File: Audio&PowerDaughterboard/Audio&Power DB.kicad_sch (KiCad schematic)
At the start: 7 parts, among them J1 AudioJack3, J2 AudioJack3, J3 AudioJack3, J4 USB_C_Receptacle_USB2.0, U1 SGTL5000XNLA3

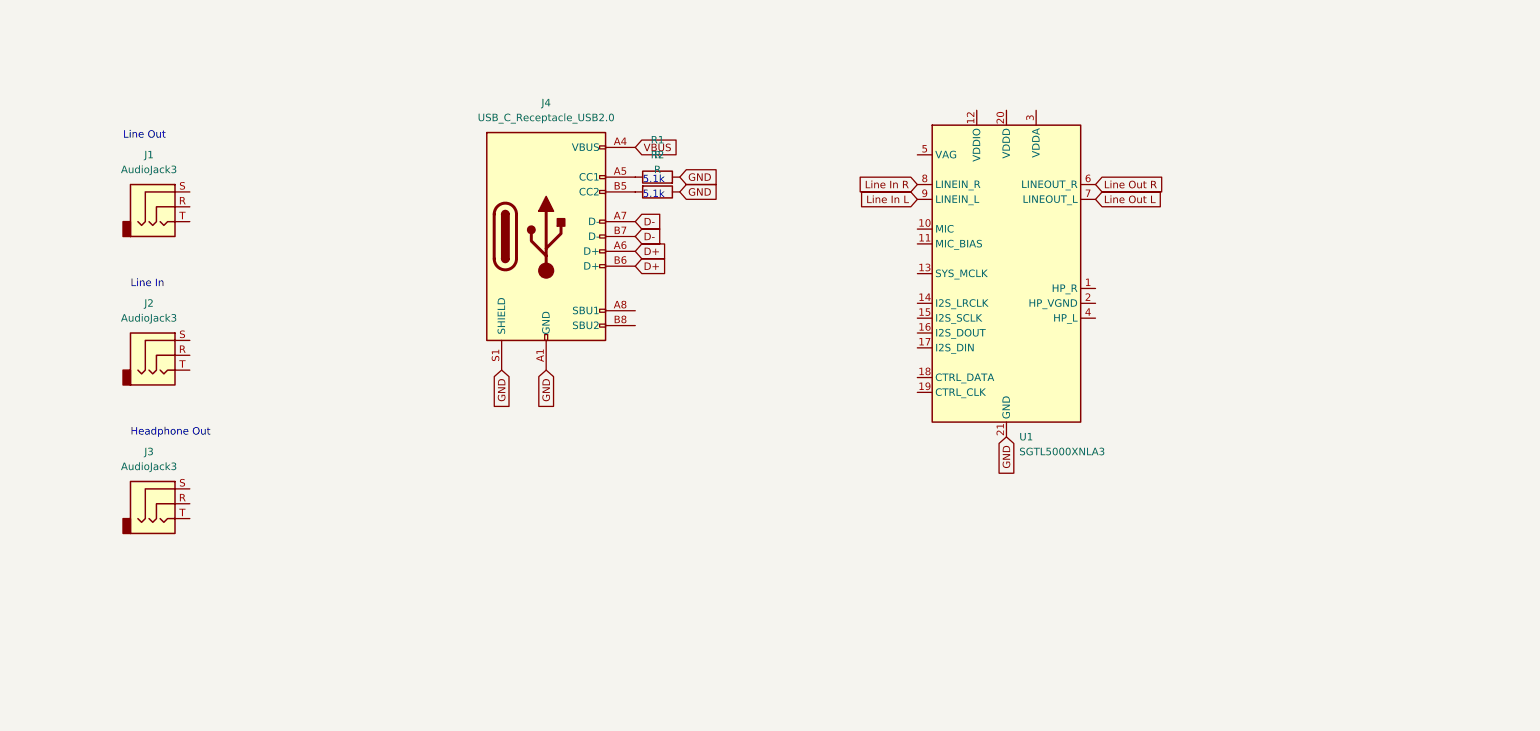
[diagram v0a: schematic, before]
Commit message: VAL FIX POWER PLS
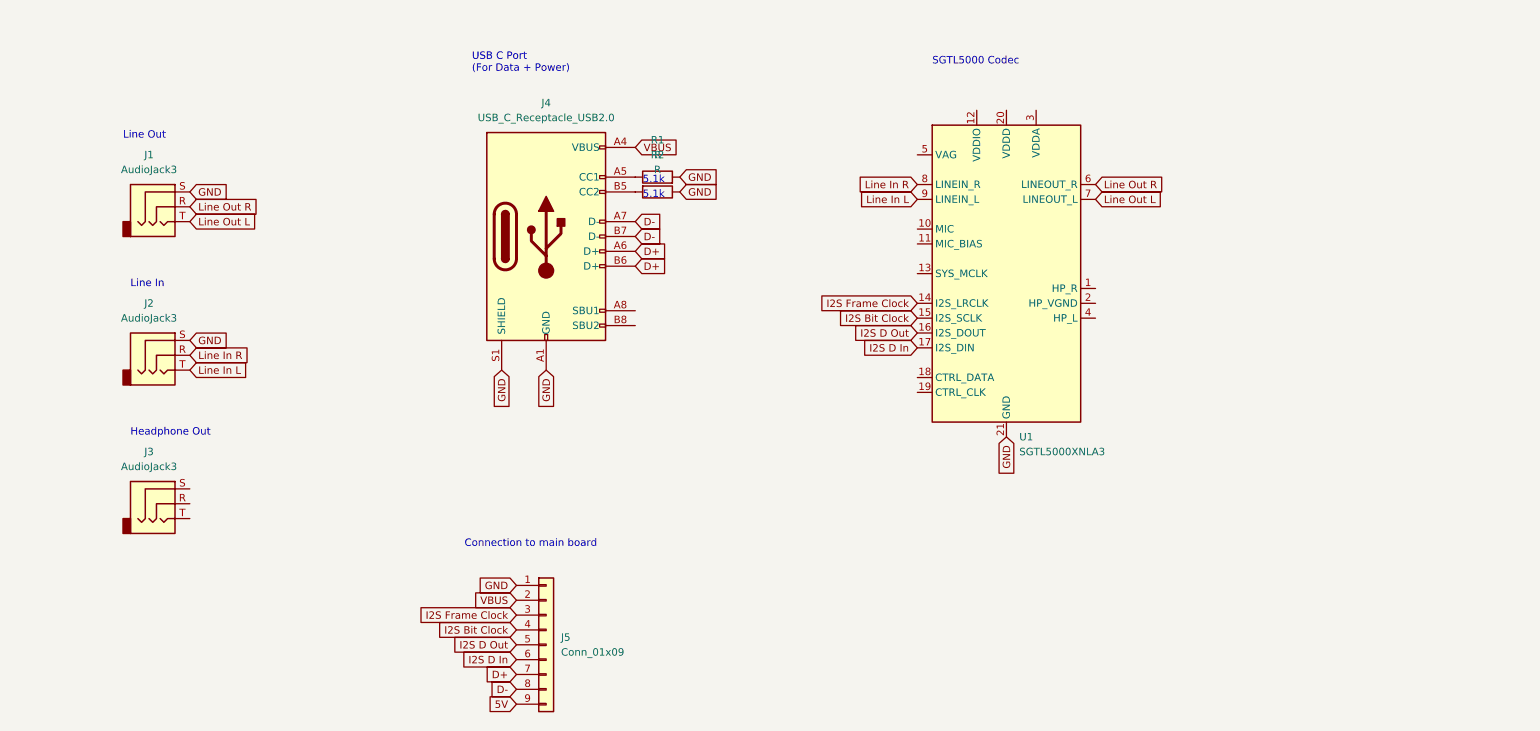
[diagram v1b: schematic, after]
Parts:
- added J5: Conn_01x09, symbol Connector_Generic:Conn_01x09
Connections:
- net D+: now also J5.7 (Pin_7)
- net D-: now also J5.8 (Pin_8)
- net GND: now also J1.S, J2.S, J5.1 (Pin_1)
- net Line In L: now also J2.T
- net Line In R: now also J2.R
- net Line Out L: now also J1.T
- net Line Out R: now also J1.R
- net VBUS: now also J5.2 (Pin_2)
- net I2S Frame Clock: now reaches U1.14 (I2S_LRCLK)
- net I2S Frame Clock: now also J5.3 (Pin_3)
- net I2S Bit Clock: now reaches U1.15 (I2S_SCLK)
- net I2S Bit Clock: now also J5.4 (Pin_4)
- net I2S D Out: now reaches U1.16 (I2S_DOUT)
- net I2S D Out: now also J5.5 (Pin_5)
- net I2S D In: now reaches U1.17 (I2S_DIN)
- net I2S D In: now also J5.6 (Pin_6)
- new net 5V: J5.9 (Pin_9)
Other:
- note added: "Connection to main board"
- note added: "SGTL5000 Codec"
- note added: "USB C Port (For Data + Power)"
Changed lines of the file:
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@@
+    (effects (font (size 1.27 1.27)) (justify left bottom))
+  )
+  (text "USB C Port\n(For Data + Power)" (at 99.06 25.4 0)
     (effects (font (size 1.27 1.27)) (justify left bottom))
   )
@@
     (effects (font (size 1.27 1.27)) (justify left bottom))
   )
+  (text "SGTL5000 Codec" (at 177.8 24.13 0)
+    (effects (font (size 1.27 1.27)) (justify left bottom))
+  )
   (text "Line Out" (at 39.37 36.83 0)
     (effects (font (size 1.27 1.27)) (justify left bottom))
   )
+  (text "Connection to main board" (at 97.79 106.68 0)
+    (effects (font (size 1.27 1.27)) (justify left bottom))
+  )
   (global_label "D-" (shape input) (at 127 53.34 0) (fields_autoplaced)
     (effects (font (size 1.27 1.27)) (justify left))
@@
     )
   )
+  (global_label "I2S D Out" (shape input) (at 175.26 69.85 180) (fields_autoplaced)
+    (effects (font (size 1.27 1.27)) (justify right))
+    (property "Intersheetrefs" "${INTERSHEET_REFS}" (at 162.8406 69.85 0)
+      (effects (font (size 1.27 1.27)) (justify right) hide)
+    )
+  )
+  (global_label "I2S Bit Clock" (shape input) (at 106.68 120.65 180) (fields_autoplaced)
+    (effects (font (size 1.27 1.27)) (justify right))
+    (property "Intersheetrefs" "${INTERSHEET_REFS}" (at 90.9344 120.65 0)
+      (effects (font (size 1.27 1.27)) (justify right) hide)
+    )
+  )
   (global_label "GND" (shape input) (at 134.62 43.18 0) (fields_autoplaced)
     (effects (font (size 1.27 1.27)) (justify left))
@@
     )
   )
+  (global_label "5V" (shape input) (at 106.68 133.35 180) (fields_autoplaced)
+    (effects (font (size 1.27 1.27)) (justify right))
+    (property "Intersheetrefs" "${INTERSHEET_REFS}" (at 101.3967 133.35 0)
+      (effects (font (size 1.27 1.27)) (justify right) hide)
+    )
+  )
+  (global_label "I2S Frame Clock" (shape input) (at 175.26 64.77 180) (fields_autoplaced)
+    (effects (font (size 1.27 1.27)) (justify right))
+    (property "Intersheetrefs" "${INTERSHEET_REFS}" (at 156.3092 64.77 0)
+      (effects (font (size 1.27 1.27)) (justify right) hide)
+    )
+  )
+  (global_label "D+" (shape input) (at 106.68 128.27 180) (fields_autoplaced)
+    (effects (font (size 1.27 1.27)) (justify right))
+    (property "Intersheetrefs" "${INTERSHEET_REFS}" (at 100.8524 128.27 0)
+      (effects (font (size 1.27 1.27)) (justify right) hide)
+    )
+  )
+  (global_label "I2S D Out" (shape input) (at 106.68 123.19 180) (fields_autoplaced)
+    (effects (font (size 1.27 1.27)) (justify right))
+    (property "Intersheetrefs" "${INTERSHEET_REFS}" (at 94.2606 123.19 0)
+      (effects (font (size 1.27 1.27)) (justify right) hide)
+    )
+  )
+  (global_label "VBUS" (shape input) (at 106.68 115.57 180) (fields_autoplaced)
+    (effects (font (size 1.27 1.27)) (justify right))
+    (property "Intersheetrefs" "${INTERSHEET_REFS}" (at 98.7962 115.57 0)
+      (effects (font (size 1.27 1.27)) (justify right) hide)
+    )
+  )
+  (global_label "I2S D In" (shape input) (at 106.68 125.73 180) (fields_autoplaced)
+    (effects (font (size 1.27 1.27)) (justify right))
+    (property "Intersheetrefs" "${INTERSHEET_REFS}" (at 95.712 125.73 0)
+      (effects (font (size 1.27 1.27)) (justify right) hide)
+    )
+  )
   (global_label "Line In L" (shape input) (at 175.26 46.99 180) (fields_autoplaced)
     (effects (font (size 1.27 1.27)) (justify right))
@@
     )
   )
+  (global_label "D-" (shape input) (at 106.68 130.81 180) (fields_autoplaced)
+    (effects (font (size 1.27 1.27)) (justify right))
+    (property "Intersheetrefs" "${INTERSHEET_REFS}" (at 100.8524 130.81 0)
+      (effects (font (size 1.27 1.27)) (justify right) hide)
+    )
+  )
+  (global_label "I2S Bit Clock" (shape input) (at 175.26 67.31 180) (fields_autoplaced)
+    (effects (font (size 1.27 1.27)) (justify right))
+    (property "Intersheetrefs" "${INTERSHEET_REFS}" (at 159.5144 67.31 0)
+      (effects (font (size 1.27 1.27)) (justify right) hide)
+    )
+  )
+  (global_label "GND" (shape input) (at 50.8 45.72 0) (fields_autoplaced)
+    (effects (font (size 1.27 1.27)) (justify left))
+    (property "Intersheetrefs" "${INTERSHEET_REFS}" (at 57.6557 45.72 0)
+      (effects (font (size 1.27 1.27)) (justify left) hide)
+    )
+  )
   (global_label "Line In R" (shape input) (at 175.26 44.45 180) (fields_autoplaced)
     (effects (font (size 1.27 1.27)) (justify right))
@@
     )
   )
+  (global_label "Line Out R" (shape input) (at 50.8 48.26 0) (fields_autoplaced)
+    (effects (font (size 1.27 1.27)) (justify left))
+    (property "Intersheetrefs" "${INTERSHEET_REFS}" (at 64.0661 48.26 0)
+      (effects (font (size 1.27 1.27)) (justify left) hide)
+    )
+  )
+  (global_label "Line Out L" (shape input) (at 50.8 50.8 0) (fields_autoplaced)
+    (effects (font (size 1.27 1.27)) (justify left))
+    (property "Intersheetrefs" "${INTERSHEET_REFS}" (at 63.8242 50.8 0)
+      (effects (font (size 1.27 1.27)) (justify left) hide)
+    )
+  )
+  (global_label "GND" (shape input) (at 50.8 71.12 0) (fields_autoplaced)
+    (effects (font (size 1.27 1.27)) (justify left))
+    (property "Intersheetrefs" "${INTERSHEET_REFS}" (at 57.6557 71.12 0)
+      (effects (font (size 1.27 1.27)) (justify left) hide)
+    )
+  )
+  (global_label "I2S D In" (shape input) (at 175.26 72.39 180) (fields_autoplaced)
+    (effects (font (size 1.27 1.27)) (justify right))
+    (property "Intersheetrefs" "${INTERSHEET_REFS}" (at 164.292 72.39 0)
+      (effects (font (size 1.27 1.27)) (justify right) hide)
+    )
+  )
+  (global_label "I2S Frame Clock" (shape input) (at 106.68 118.11 180) (fields_autoplaced)
+    (effects (font (size 1.27 1.27)) (justify right))
+    (property "Intersheetrefs" "${INTERSHEET_REFS}" (at 87.7292 118.11 0)
+      (effects (font (size 1.27 1.27)) (justify right) hide)
+    )
+  )
   (global_label "VBUS" (shape input) (at 127 38.1 0) (fields_autoplaced)
     (effects (font (size 1.27 1.27)) (justify left))
@@
     )
   )
+  (global_label "Line In R" (shape input) (at 50.8 73.66 0) (fields_autoplaced)
+    (effects (font (size 1.27 1.27)) (justify left))
+    (property "Intersheetrefs" "${INTERSHEET_REFS}" (at 62.6147 73.66 0)
+      (effects (font (size 1.27 1.27)) (justify left) hide)
+    )
+  )
   (global_label "GND" (shape input) (at 111.76 76.2 270) (fields_autoplaced)
     (effects (font (size 1.27 1.27)) (justify right))
@@
     (property "Intersheetrefs" "${INTERSHEET_REFS}" (at 190.5 94.4857 90)
       (effects (font (size 1.27 1.27)) (justify right) hide)
+    )
+  )
+  (global_label "GND" (shape input) (at 106.68 113.03 180) (fields_autoplaced)
+    (effects (font (size 1.27 1.27)) (justify right))
+    (property "Intersheetrefs" "${INTERSHEET_REFS}" (at 99.8243 113.03 0)
+      (effects (font (size 1.27 1.27)) (justify right) hide)
+    )
+  )
+  (global_label "Line In L" (shape input) (at 50.8 76.2 0) (fields_autoplaced)
+    (effects (font (size 1.27 1.27)) (justify left))
+    (property "Intersheetrefs" "${INTERSHEET_REFS}" (at 62.3728 76.2 0)
+      (effects (font (size 1.27 1.27)) (justify left) hide)
     )
   )
@@
         )
       )
+    )
+  )
+  (symbol (lib_id "Connector_Generic:Conn_01x09") (at 111.76 123.19 0) (unit 1)
+    (in_bom yes) (on_board yes) (dnp no) (fields_autoplaced)
+    (property "Reference" "J5" (at 114.3 121.92 0)
+      (effects (font (size 1.27 1.27)) (justify left))
+    )
+    (property "Value" "Conn_01x09" (at 114.3 124.46 0)
+      (effects (font (size 1.27 1.27)) (justify left))
+    )
+    (property "Footprint" "" (at 111.76 123.19 0)
+      (effects (font (size 1.27 1.27)) hide)
+    )
+    (property "Datasheet" "~" (at 111.76 123.19 0)
+      (effects (font (size 1.27 1.27)) hide)
+    )
+    (pin "1")
+    (pin "2")
+    (pin "3")
+    (pin "4")
+    (pin "5")
+    (pin "6")
+    (pin "7")
+    (pin "8")
+    (pin "9")
+    (instances
+      (project "Audio&Power DB"
+        (path "/efee3861-08c8-4ee5-870a-4ef6b30a8ea3"
+          (reference "J5") (unit 1)
+        )
+      )

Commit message: Power Daughterboard fully revised
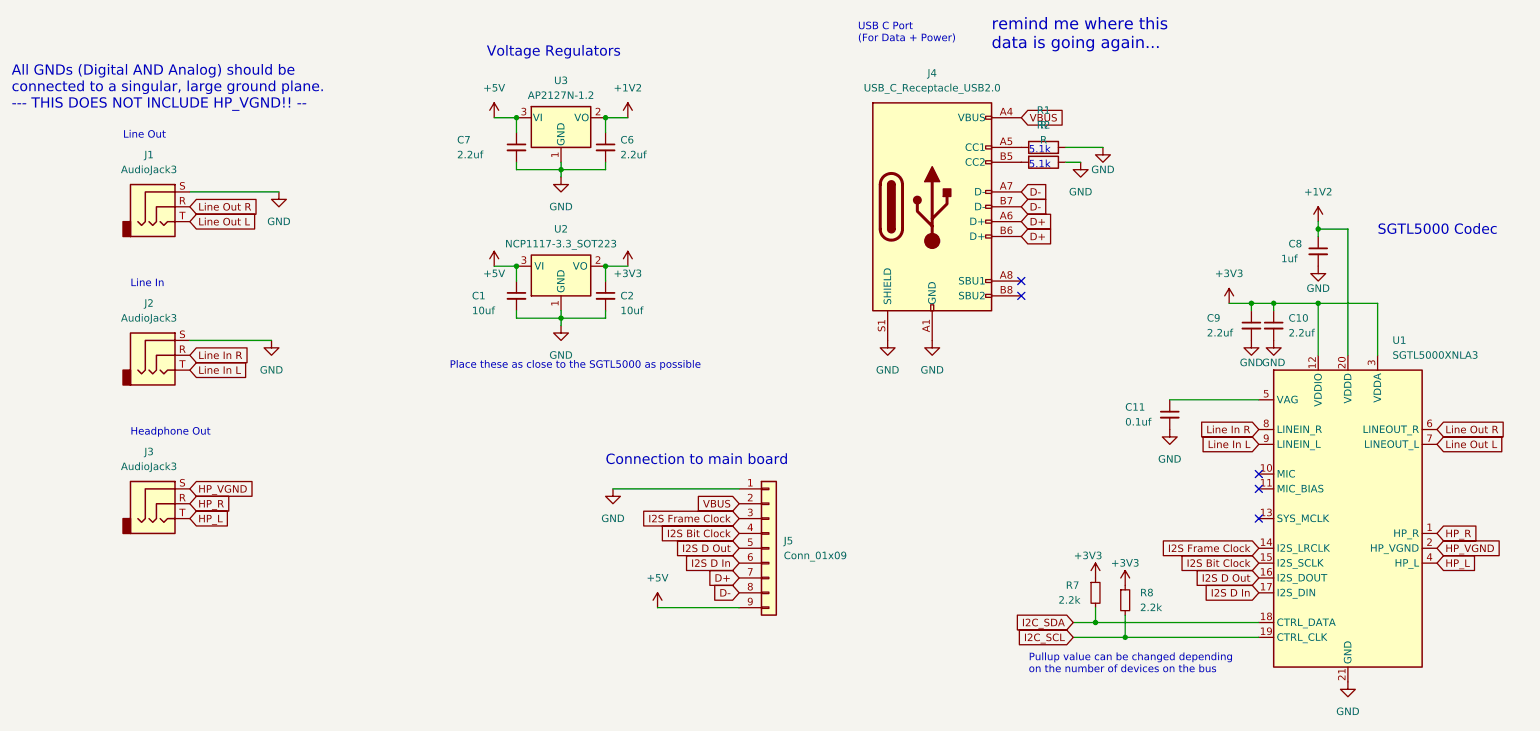
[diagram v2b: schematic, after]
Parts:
- added C1, C2: 10uf, symbol Device:C_Small
- added C10, C6, C7, C9: 2.2uf, symbol Device:C_Small
- added C11: 0.1uf, symbol Device:C_Small
- added C8: 1uf, symbol Device:C_Small
- added R7, R8: 2.2k, symbol Device:R_Small
- added U2: NCP1117-3.3_SOT223, Package_TO_SOT_SMD:SOT-223-3_TabPin2, symbol Regulator_Linear:NCP1117-3.3_SOT223
- added U3: AP2127N-1.2, Package_TO_SOT_SMD:SOT-23, symbol Regulator_Linear:AP2127N-1.2
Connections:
- net GND: now also C1.2, C10.2, C11.2, C2.2, C6.2, C7.2, C8.2, C9.2, U2.1 (GND), U3.1 (GND)
- net HP_R: now reaches U1.1 (HP_R)
- net HP_R: now also J3.R
- net +3V3: now reaches U1.12 (VDDIO)
- net +3V3: now also U1.3 (VDDA), C10.1, C2.1, C9.1, R7.1, R8.1, U2.2 (VO)
- net I2C_SDA: now reaches U1.18 (CTRL_DATA)
- net I2C_SDA: now also R7.2
- net I2C_SCL: now reaches U1.19 (CTRL_CLK)
- net I2C_SCL: now also R8.2
- net HP_VGND: now reaches U1.2 (HP_VGND)
- net HP_VGND: now also J3.S
- net +1V2: now reaches U1.20 (VDDD)
- net +1V2: now also C6.1, C8.1, U3.2 (VO)
- net HP_L: now reaches U1.4 (HP_L)
- net HP_L: now also J3.T
- net at U1.5 (VAG): now also C11.1
- net 5V renamed +5V
- net +5V: now also C1.1, C7.1, U2.3 (VI), U3.3 (VI)
- no-connect marks 0 -> 5
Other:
- note added: "All GNDs (Digital AND Analog) should be connected to a singular, large ground plane. --- THIS DOES NOT INCLUDE HP_VGND!! --"
- note added: "Place these as close to the SGTL5000 as possible"
- note added: "Pullup value can be changed depending on the number of devices on the bus"
- note added: "Voltage Regulators"
- note added: "remind me where this data is going again..."
- title: (none) -> Audio and Power Daughterboard
- moved on the sheet: J4, J5, R1, R2, U1
